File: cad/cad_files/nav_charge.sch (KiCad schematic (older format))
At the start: 13 parts

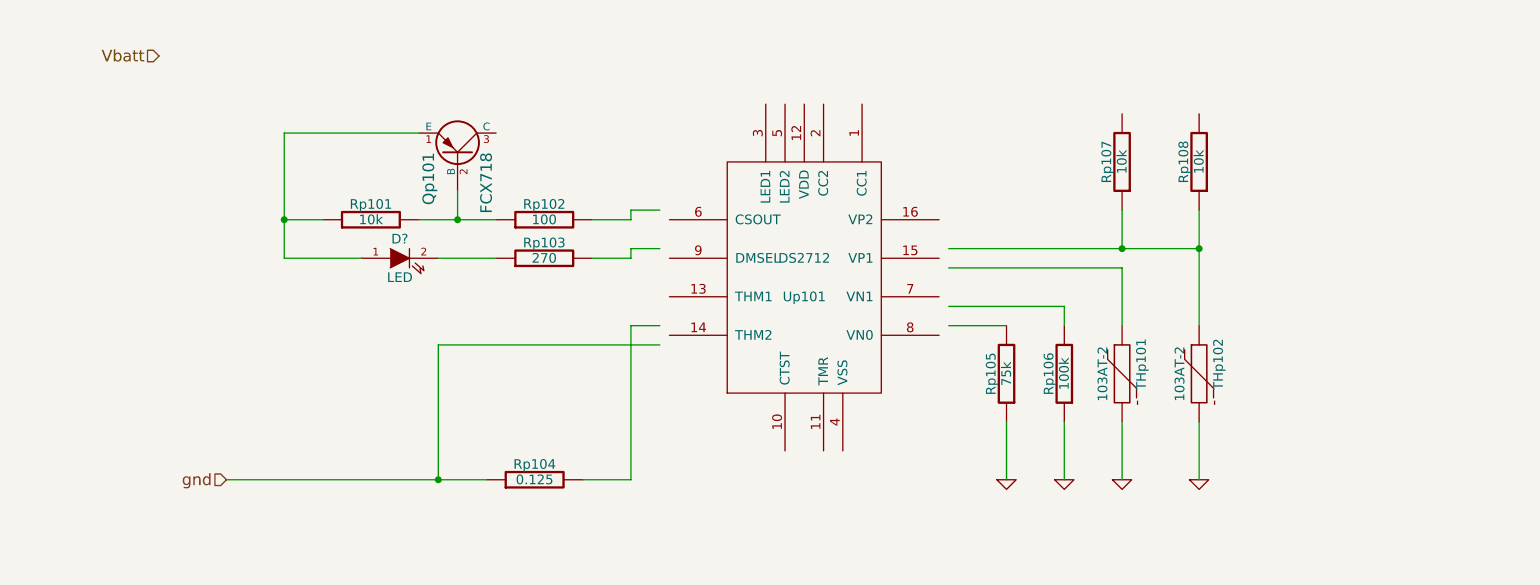
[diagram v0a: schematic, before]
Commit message: DS2712 circuit, somewhat
datasheet fig.3 - lacks current regulation
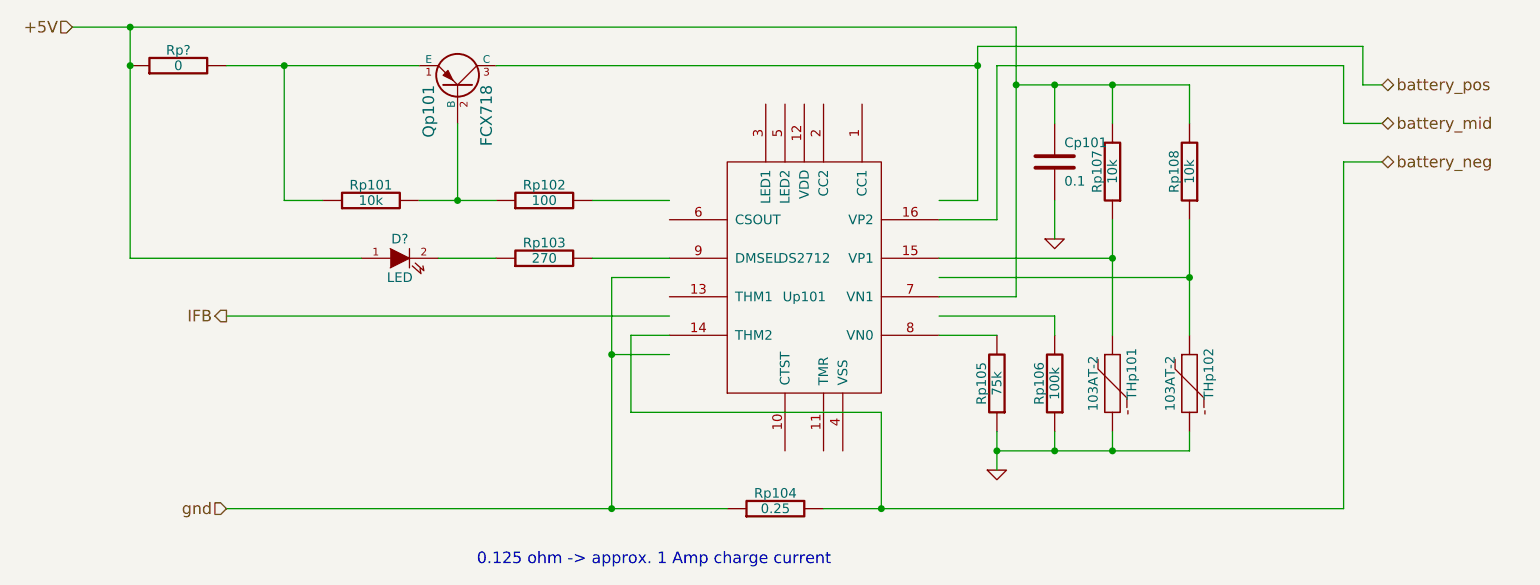
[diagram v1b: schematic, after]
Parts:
- added Cp101: 0.1, symbol C
- added Rp?: 0, symbol R
- Rp104: value 0.125 -> 0.25
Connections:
- net labels added: +5V, IFB, battery_mid, battery_neg, battery_pos
- net labels removed: Vbatt
- wire segments 31 -> 53
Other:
- note added: "0.125 ohm -> approx. 1 Amp charge current"
- moved on the sheet: Qp101, Rp101, Rp102, Rp104, Rp105, Rp106, Rp107, Rp108, THp101, THp102

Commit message: NiMH Battery Charging update
* DS2712 charger, 2S configuration,
* circuit modeled on eval board schematic
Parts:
- added BT1, BT2: BATTERY, symbol BATTERY
- added C? (x2): 47uF, symbol C
- added C?: 0.1uF, symbol C
- added C?: 1uF, symbol C
- added D?: ZENER, symbol ZENER
- added D? (x2): DIODE, symbol DIODE
- added D?: LED, symbol LED
- added L?: 47uH, symbol INDUCTOR
- added P?: CONN_5, symbol CONN_5
- added Q?: ZXM62P02E6, symbol MOSFET_P
- added Qp? (x2): FCX718, symbol PNP
- added R10: 10, symbol R
- added R14: .075, symbol R
- added R?: R, symbol R
- added Rp?: 330, symbol R
- added Rp?: 0, symbol R
- added Rp?: 270, symbol R
- added Rp?: 100, symbol R
- added Rp?: 10k, symbol R
- added Rp?: 150, symbol R
- added Rp?: 120k, symbol R
- added Rp?: 33k, symbol R
- added Up?: DS2712, MODULE, symbol DS2712
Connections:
- net labels added: VDD, to_vn2
- net labels removed: battery_mid
- wire segments 53 -> 169
- no-connect marks 0 -> 4
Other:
- note added: "2S -> open"
- note added: "LED2 prog:\nopen for 2S\nlow for 1S\nhigh for 2P"
- note added: "WHY!?"
- note added: "check value"
- moved on the sheet: Cp101, D?, Qp101, Rp101, Rp102, Rp103, Rp104, Rp105, Rp106, Rp107, Rp108, Rp?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

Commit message: removing old charging circuit
updating/fixing up new circuit (from app-note)
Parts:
- removed C?: 47uF, symbol C
- removed D?: ZENER, symbol ZENER
- removed Qp?: FCX718, symbol PNP
- removed R?: R, symbol R
- added Rp?: 0.25, symbol R
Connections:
- net labels removed: IFB, to_vn2
- wire segments 169 -> 123
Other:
- moved on the sheet: BT1, BT2, C?, Cp101, D?, L?, Q?, Qp101, Qp?, R10, R14, Rp101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

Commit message: charger schematic work
* modify DS2712 schematic element
  - pin locations
* sheet I/O ``pins'' updating
* adding notes/comments
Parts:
- removed Cp101: 0.1, symbol C
- removed D?: LED, symbol LED
- removed P?: CONN_5, symbol CONN_5
- removed Qp101: FCX718, symbol PNP
- removed Rp101: 10k, symbol R
- removed Rp102: 100, symbol R
- removed Rp103: 270, symbol R
- removed Rp104, Rp?: 0.25, symbol R
- removed Rp105: 75k, symbol R
- removed Rp106: 100k, symbol R
- removed Rp?: 0, symbol R
- removed Up101: DS2712, MODULE, symbol DS2712
- R14: value .075 -> .27
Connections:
- net labels added: CC1a, CC1b, CHG_V_a, CHG_V_b, Ctst, ICHG_a, ICHG_b, ICHG_c, ICHG_d, LED_1a, LED_1b, TMR, VN_H, VP1, VP2, chgr_gnd, thm1, thm2
- net labels removed: VDD, gnd
- wire segments 123 -> 75
- no-connect marks 4 -> 2
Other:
- note added: "TODO: power path for charger voltage rail \n (rather than cutting load power \n while charging)"
- note added: "Voltage across VN0-VN1 -> 0.125 Volt\n0.27 ohm -> approx. 0.45 Amp\n0.125 ohm -> approx. 1 Amp charge current\n\n(0.125 / Rsense) * 0.969 -> charge current"
- note removed: "0.125 ohm -> approx. 1 Amp charge current"
- note removed: "2S -> open"
- note removed: "check value"
